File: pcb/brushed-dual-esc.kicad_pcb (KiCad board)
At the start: 2 copper layers, 29.5 x 25 mm, 24 parts, among them J1 XT30PW-M, J2 Conn_02x03_Odd_Even, J3 TC2030-NL, J6 XT30PW-F, J7 XT30PW-F, U2 AZ1117-5.0, U3 STM32C011F4Ux, U4 DRV8231ADSGR, U5 TLV77133PDBVR, U6 DRV8231ADSGR

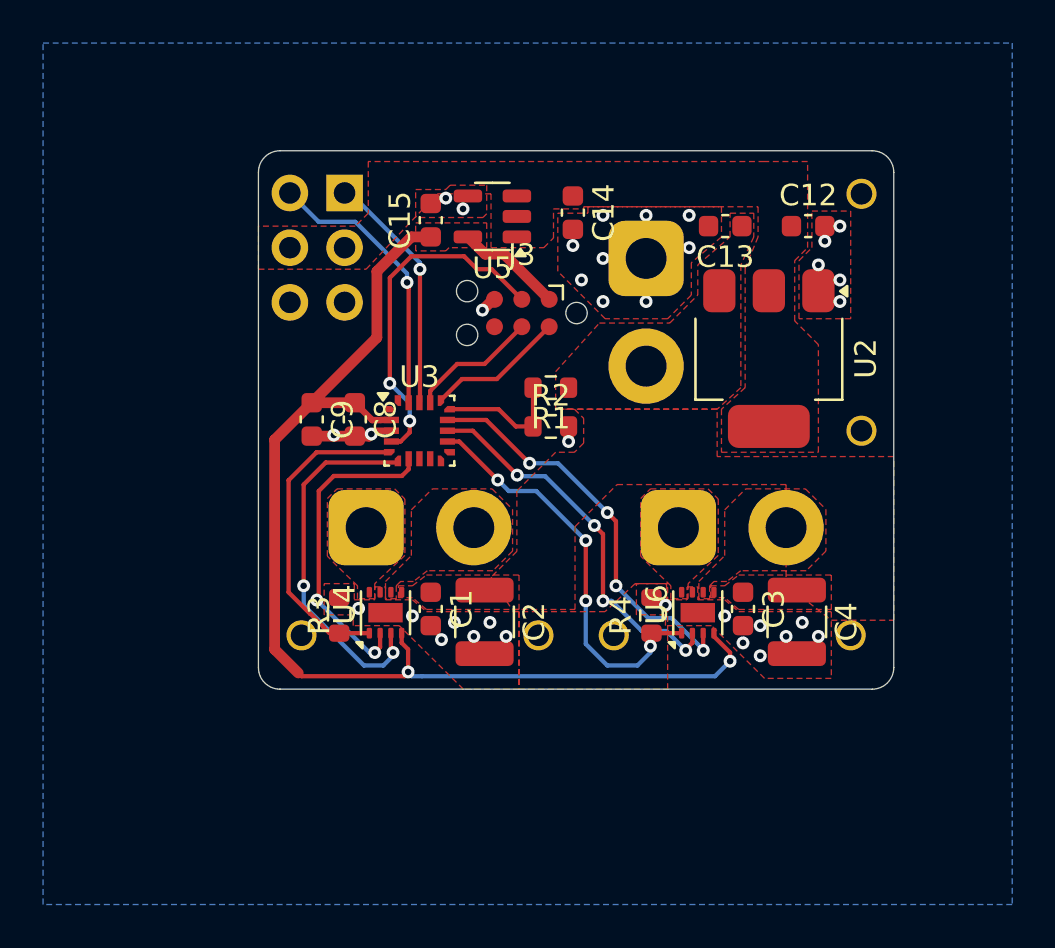
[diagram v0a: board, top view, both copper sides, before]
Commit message: Add status LED on spare pin
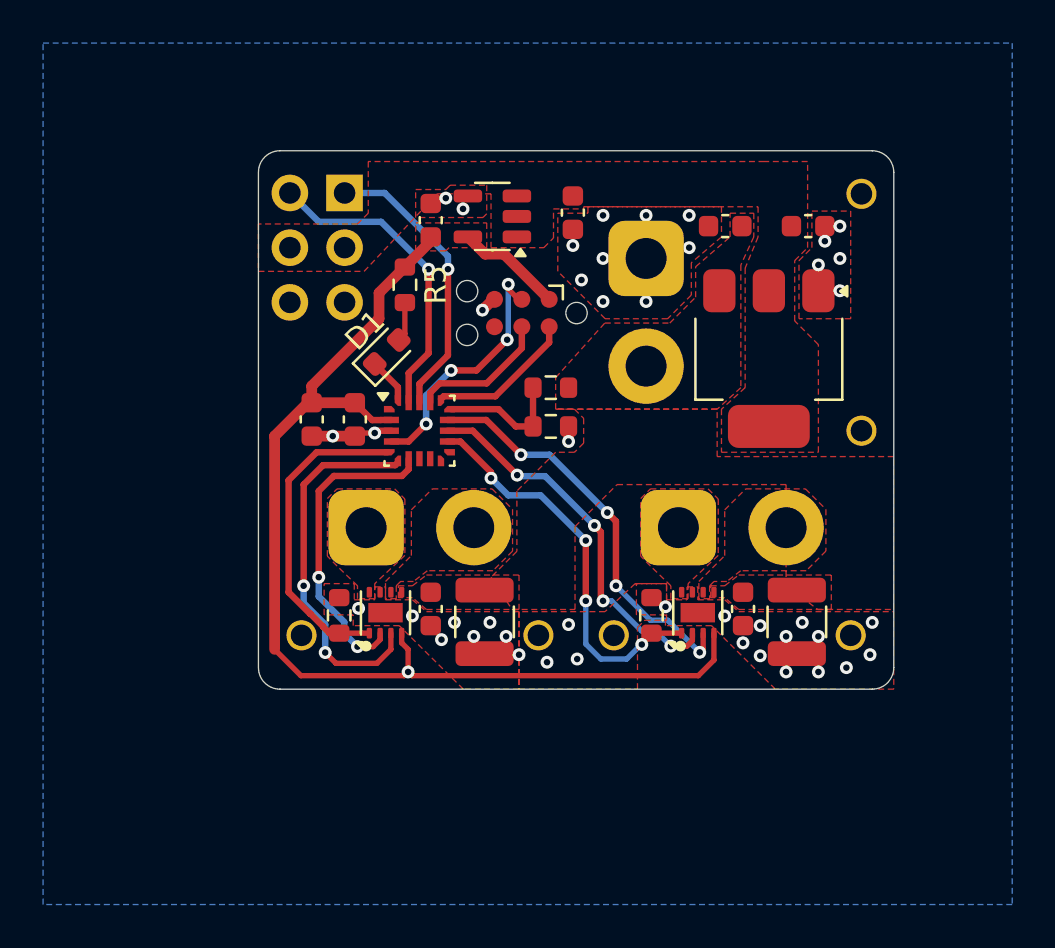
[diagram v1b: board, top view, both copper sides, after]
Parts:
- added D1: B1911USD, LED_SMD:LED_0603_1608Metric, F.Cu at (126.0, 84.3)
- added R5: 270, Resistor_SMD:R_0603_1608Metric, F.Cu at (126.8, 81.2)
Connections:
- J6 pad : GND -> (no net)
- J7 pad : GND -> (no net)
- U3 pad 20: unconnected-(U3-PC14-Pad20) -> /LED
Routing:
- net /~{RESET}: track 16.0 -> 11.9 mm, vias 2 -> 4
- net /LED: track 0.00 -> 2.07 mm
- net /RX_CH2: track 11.4 -> 13.4 mm
- net Net-(D1-A): track 0.00 -> 1.85 mm
- net +3V3: track 57.4 -> 55.9 mm, vias 2 -> 1
- net /RX_CH1: track 13.1 -> 14.5 mm
- net /DRV2_ISENSE: track 19.1 -> 18.6 mm
- net /SWCLK: track 6.04 -> 6.57 mm
- net GND: track 5.31 -> 5.34 mm, vias 35 -> 44

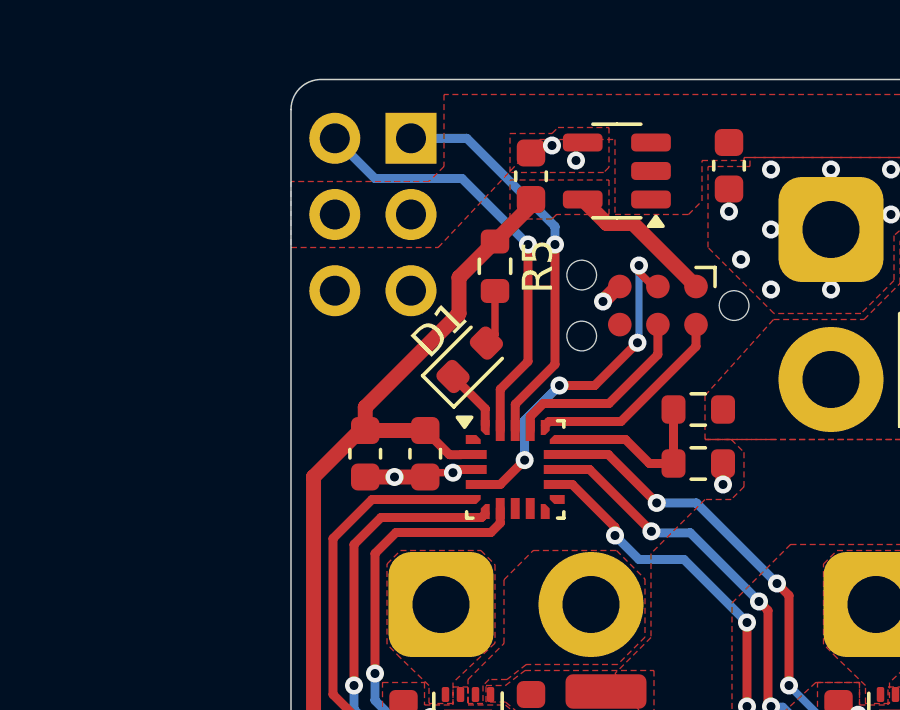
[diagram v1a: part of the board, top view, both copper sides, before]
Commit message: Create 3V3 zone in top left
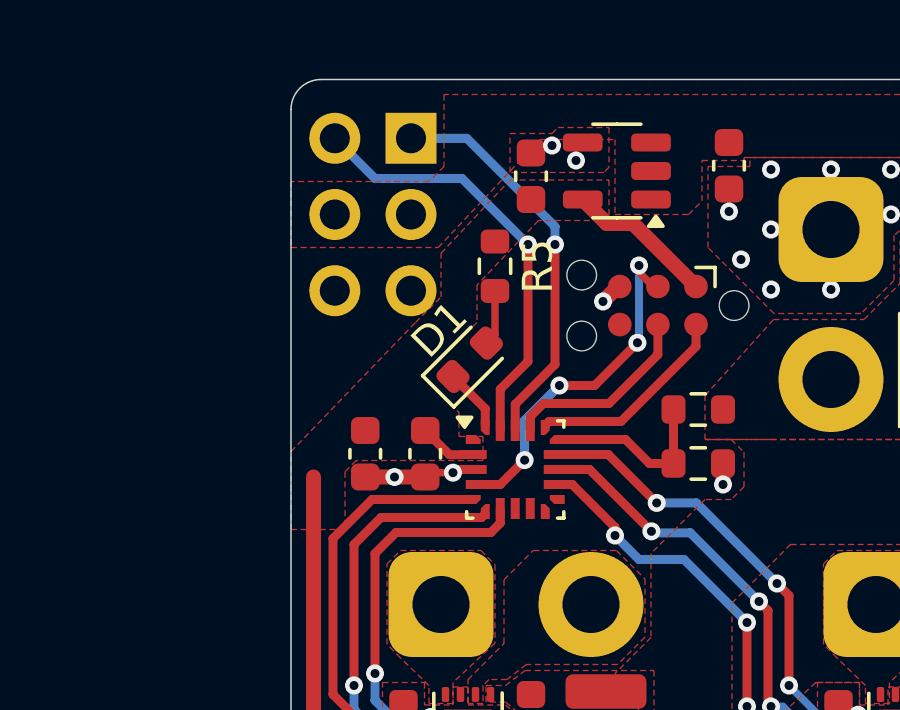
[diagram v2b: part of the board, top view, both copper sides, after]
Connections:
- J6 pad : (no net) -> GND
- J7 pad : (no net) -> GND
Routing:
- net +3V3: track 55.9 -> 41.9 mm

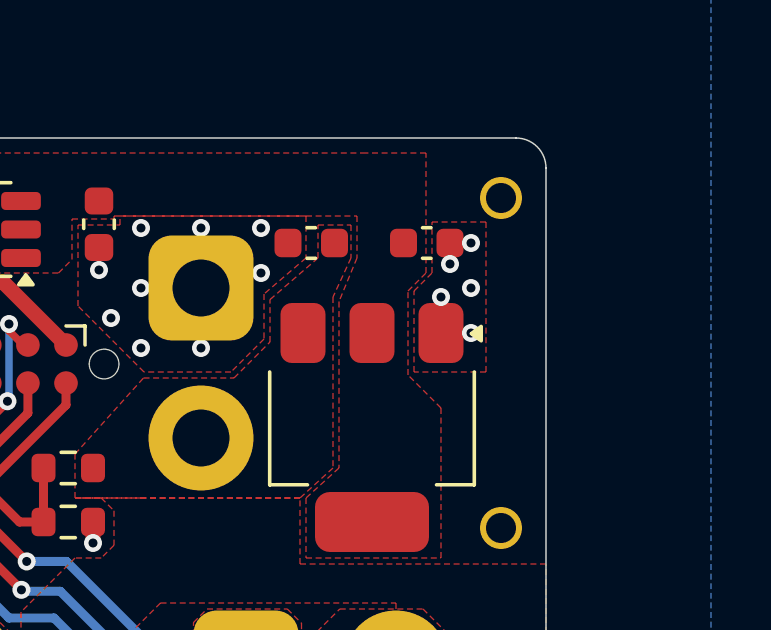
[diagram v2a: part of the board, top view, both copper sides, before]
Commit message: Adjust 5V LDO ground plane placement
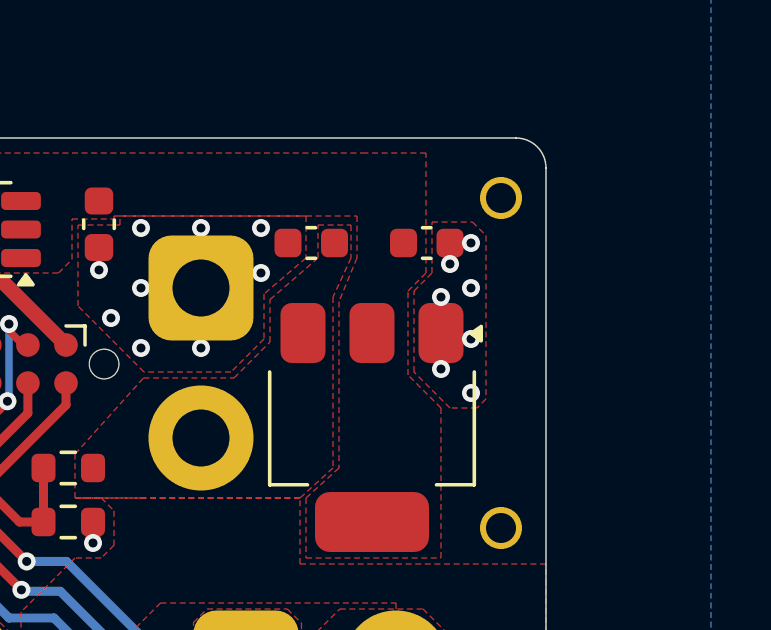
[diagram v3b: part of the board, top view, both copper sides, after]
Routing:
- net GND: vias 44 -> 46

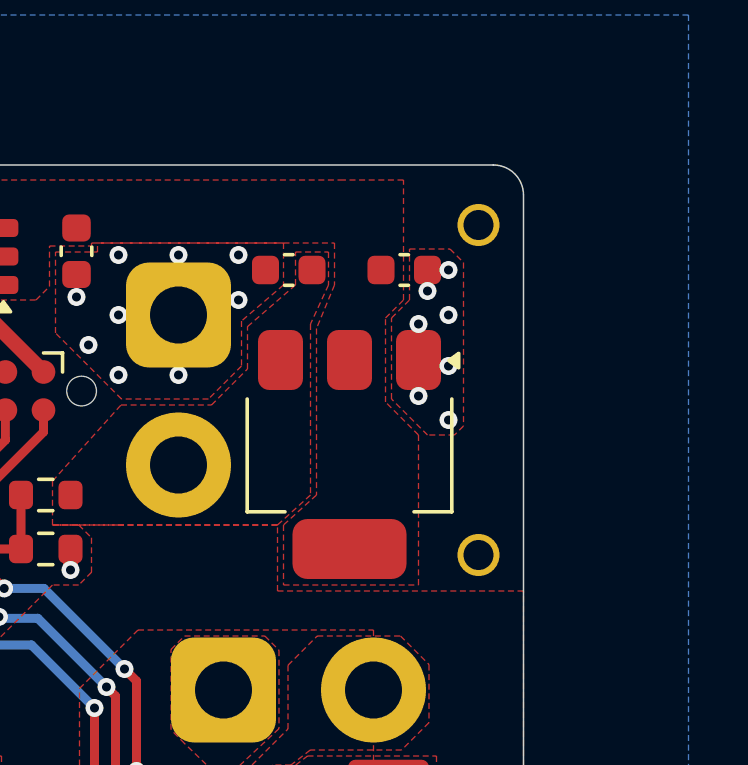
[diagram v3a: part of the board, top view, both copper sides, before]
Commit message: Increase top GND zone size for LDO
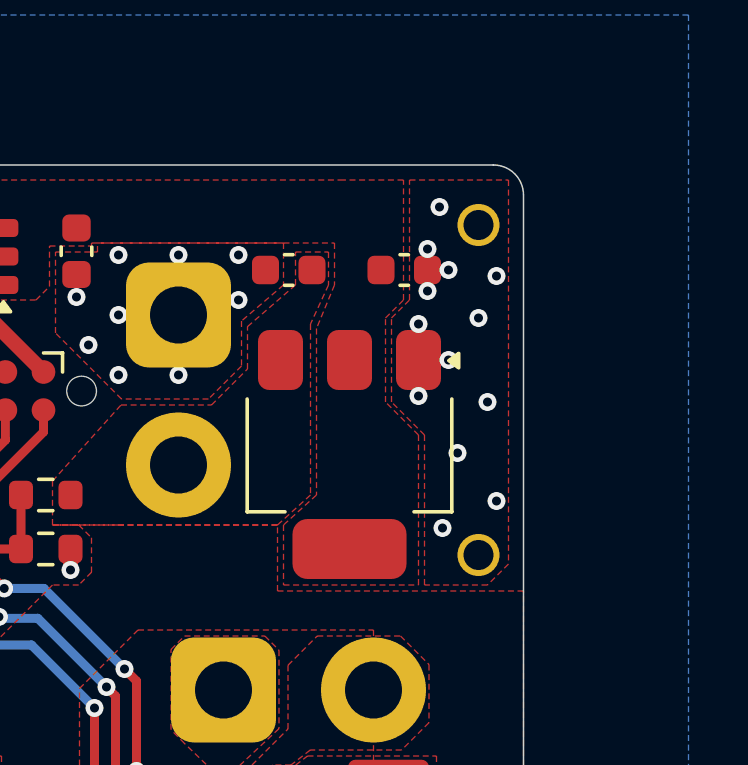
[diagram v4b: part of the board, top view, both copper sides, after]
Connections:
- J1 pad : (no net) -> GND
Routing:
- net GND: vias 46 -> 52

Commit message: Fix capacitor siutation
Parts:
- removed the C1 at (128.0, 96.3)
- removed the C3 at (142.5, 96.3)
- removed C4: 47u, Capacitor_SMD:C_1210_3225Metric
- added C10: UMK107BJ105KA-T, Capacitor_SMD:C_0603_1608Metric, F.Cu at (142.6, 96.4)
- added C11: UMK107BJ105KA-T, Capacitor_SMD:C_0603_1608Metric, F.Cu at (144.3, 96.4)
- added C12: UMK107BJ105KA-T, Capacitor_SMD:C_0603_1608Metric, F.Cu at (146.0, 96.4)
- added C13: UMK107BJ105KA-T, Capacitor_SMD:C_0603_1608Metric, F.Cu at (128.0, 78.2)
- added C16: UMK107BJ105KA-T, Capacitor_SMD:C_0603_1608Metric, F.Cu at (124.0, 87.3)
- added C17: UMK107BJ105KA-T, Capacitor_SMD:C_0603_1608Metric, F.Cu at (122.0, 87.3)
- added C7: UMK107BJ105KA-T, Capacitor_SMD:C_0603_1608Metric, F.Cu at (128.1, 96.4)
- added G***: LOGO, LOGO, B.Cu at (134.6, 89.3)
- added kibuzzard-68AE1D03: G***, kibuzzard-68AE1D03, B.Cu at (127.7, 82.0)
- added kibuzzard-68AE1D1E: G***, kibuzzard-68AE1D1E, B.Cu at (127.7, 79.5)
- added kibuzzard-68AE1D34: G***, kibuzzard-68AE1D34, B.Cu at (121.5, 85.8)
- added kibuzzard-68AE1D4C: G***, kibuzzard-68AE1D4C, B.Cu at (124.0, 85.8)
- added kibuzzard-68AE1DA9: G***, kibuzzard-68AE1DA9, B.Cu at (127.7, 77.0)
- added kibuzzard-68AE251B: G***, kibuzzard-68AE251B, F.Cu at (139.8, 89.8)
- added kibuzzard-68AE2565: G***, kibuzzard-68AE2565, F.Cu at (142.8, 76.5)
- added kibuzzard-68AE2599: G***, kibuzzard-68AE2599, F.Cu at (147.9, 92.5)
- added kibuzzard-68AE2599: G***, kibuzzard-68AE2599, F.Cu at (133.4, 92.5)
- C1: renamed from C13; value 22u -> 22u 16V
- C14, C15: value 1u -> UMK107BJ105KA-T
- C2: value 47u -> ESS107M016AC2KA; footprint Capacitor_SMD:C_1210_3225Metric -> Capacitor_THT:CP_Radial_D5.0mm_P2.00mm; moved to B.Cu
- C3: renamed from C12; value 22u -> 22u 16V
- C8: value 100n -> UMK107BJ105KA-T
- C9: value 4.7u -> UMK107BJ105KA-T
- moved C2 14.3 mm to (135.5, 83.5), turned to 90 degrees
- moved C9 12.7 mm to (131.5, 96.4)
- moved C8 10.4 mm to (129.8, 96.4)
- moved C15 9.27 mm to (126.0, 87.3), turned to -90 degrees
- moved R1 4.20 mm to (124.2, 84.5), turned to 0 degrees
- moved U3 1.82 mm to (129.0, 87.0)
- moved D1 1.04 mm to (126.7, 83.6), turned to 90 degrees
- moved U1 0.70 mm to (143.7, 84.0)
- moved J2 0.59 mm to (131.6, 82.5)
- moved U2 0.30 mm to (131.2, 78.0)
- moved R2 0.21 mm to (133.6, 86.2)
- moved C1 0.10 mm to (141.6, 78.5)
- moved R3 0.05 mm to (133.6, 87.8)
- renumbered J3 to J2, J2 to J3, J6 to J4, J7 to J5, R5 to R1, R1 to R2, R2 to R3, R3 to R4, R4 to R5, U2 to U1, U5 to U2, U6 to U5
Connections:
- C8 pad 1: +3V3 -> +BATT
- C9 pad 1: +3V3 -> +BATT
- U3 pad 1: unconnected-(U3-PC15-Pad1) -> /LED
- U3 pad 20: /LED -> unconnected-(U3-PC14-Pad20)
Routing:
- net +3V3: track 41.9 -> 60.6 mm
- net /SWCLK: track 6.57 -> 3.48 mm
- net /SWDIO: track 6.84 -> 3.89 mm
- net /~{RESET}: track 11.9 -> 9.16 mm, vias 4 -> 2
- net /RX_CH2: track 13.4 -> 11.1 mm
- net GND: track 5.34 -> 7.49 mm, vias 52 -> 47
- net /DRV1_IN2: track 14.5 -> 16.6 mm
- net /DRV1_ISENSE: track 14.9 -> 16.8 mm
- net /DRV1_IN1: track 17.3 -> 19.2 mm
- net /BATT_SENSE: track 5.93 -> 4.01 mm
- net /RX_CH1: track 14.5 -> 12.7 mm
- net Net-(D1-A): track 1.85 -> 2.39 mm

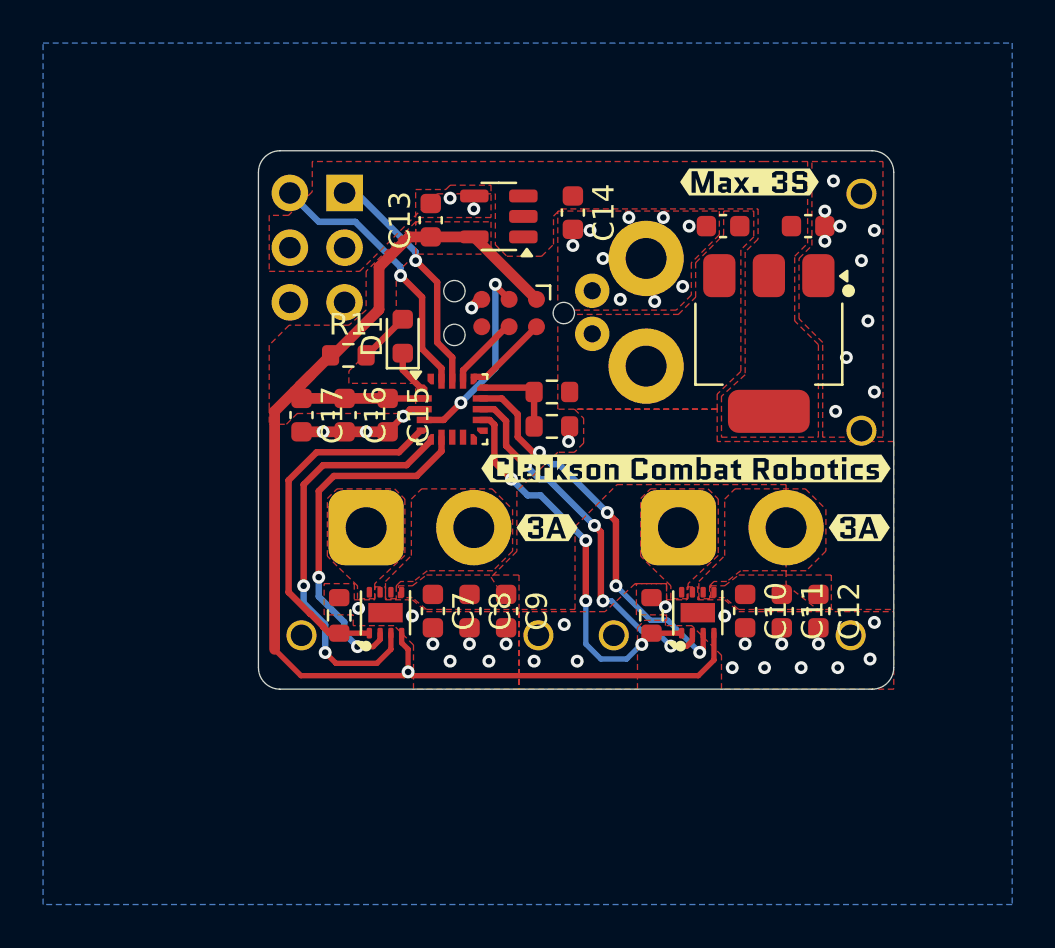
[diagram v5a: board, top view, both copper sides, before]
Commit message: Add testpoints and imrpove silkscreen
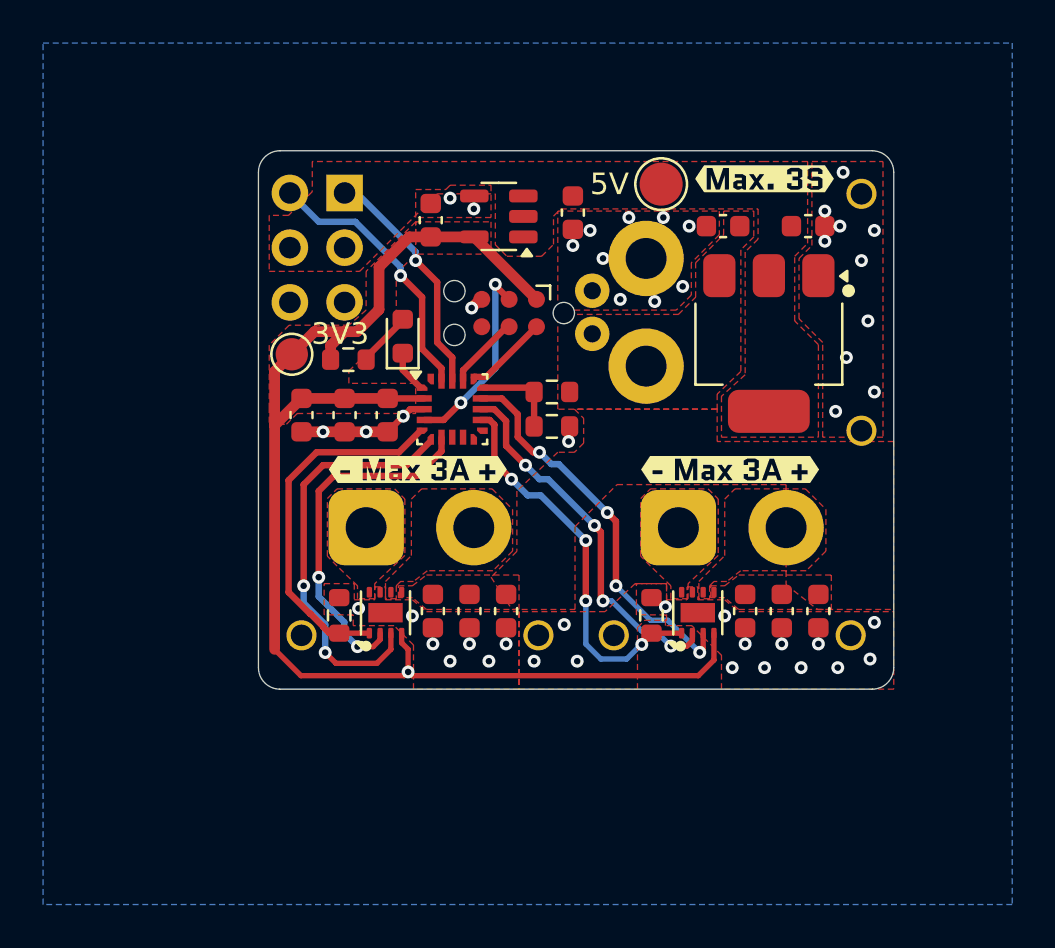
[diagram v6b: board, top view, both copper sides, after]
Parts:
- removed kibuzzard-68AE251B: G***, kibuzzard-68AE251B
- removed kibuzzard-68AE2599 (x2): G***, kibuzzard-68AE2599
- added TP1: 5V, TestPoint:TestPoint_Pad_D2.0mm, F.Cu at (138.7, 76.5)
- added TP2: 3V3, TestPoint:TestPoint_Pad_D1.5mm, F.Cu at (121.5, 84.5)
- added kibuzzard-68AE6F6F: G***, kibuzzard-68AE6F6F, B.Cu at (128.1, 86.1)
- added kibuzzard-68AF2469: G***, kibuzzard-68AF2469, F.Cu at (141.9, 89.8)
- added kibuzzard-68AF2469: G***, kibuzzard-68AF2469, F.Cu at (127.4, 89.8)
- added kibuzzard-68AF2501: G***, kibuzzard-68AF2501, B.Cu at (138.7, 76.3)
- moved kibuzzard-68AE2565 0.72 mm to (143.5, 76.3)
- moved R1 0.20 mm to (124.2, 84.7)
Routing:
- net +3V3: track 60.6 -> 63.8 mm

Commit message: Add step file
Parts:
- removed the C11 at (144.3, 96.4)
- removed the C8 at (129.8, 96.4)
- removed kibuzzard-68AE1D03: G***, kibuzzard-68AE1D03
- removed kibuzzard-68AE1D1E: G***, kibuzzard-68AE1D1E
- removed kibuzzard-68AE1D34: G***, kibuzzard-68AE1D34
- removed kibuzzard-68AE1D4C: G***, kibuzzard-68AE1D4C
- removed kibuzzard-68AE1DA9: G***, kibuzzard-68AE1DA9
- removed kibuzzard-68AE2565: G***, kibuzzard-68AE2565
- removed kibuzzard-68AE6F6F: G***, kibuzzard-68AE6F6F
- removed kibuzzard-68AF2501: G***, kibuzzard-68AF2501
- C1, C3: footprint Capacitor_SMD:C_0603_1608Metric -> Capacitor_SMD:C_0805_2012Metric
- moved C5 12.5 mm to (133.7, 95.9), turned to 0 degrees
- moved C1 8.93 mm to (142.3, 87.4), turned to 0 degrees
- moved TP1 6.91 mm to (145.6, 77.0)
- moved G*** 6.28 mm to (128.8, 86.9)
- moved C3 4.63 mm to (141.1, 77.2), turned to -90 degrees
- moved C10 2.04 mm to (144.6, 97.0)
- moved R5 2.04 mm to (140.2, 97.2)
- moved U5 2.04 mm to (142.3, 97.0)
- moved U1 1.63 mm to (144.4, 82.5), turned to 0 degrees
- moved R2 1.51 mm to (133.8, 84.7)
- moved R3 1.51 mm to (133.8, 86.3)
- moved R4 1.12 mm to (124.7, 97.2)
- moved U4 1.12 mm to (126.8, 97.0)
- moved J4 1.12 mm to (124.5, 93.5)
- moved J5 1.12 mm to (140.0, 93.5)
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- renumbered C9 to C11, C14 to C2, C13 to C4, C2 to C5, C15 to C6, C16 to C7, C17 to C8, C7 to C9
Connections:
- J1 pad : GND -> (no net)
- J4 pad : GND -> (no net)
- J5 pad : GND -> (no net)
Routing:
- net +3V3: track 63.8 -> 73.9 mm, vias 1 -> 2
- net /DRV1_IN2: track 16.6 -> 20.0 mm, vias 2 -> 0
- net /DRV2_IN1: track 18.4 -> 21.6 mm
- net /DRV2_IN2: track 17.3 -> 19.8 mm
- net /~{RESET}: track 9.16 -> 11.1 mm, vias 2 -> 4
- net /DRV1_IN1: track 19.2 -> 20.6 mm
- net /DRV1_ISENSE: track 16.8 -> 15.7 mm, vias 0 -> 3
- net GND: track 7.49 -> 8.17 mm, vias 47 -> 36
- net /DRV2_ISENSE: track 18.3 -> 18.9 mm
- net /SWCLK: track 3.48 -> 4.05 mm
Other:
- board text added: "3V3"
- board text added: "5V 1A"
- board text added: "CH1"
- board text added: "CH2"
- board text added: "Clarkson"
- board text added: "Combat Robotics"
- board text added: "Designed by Sigmond Kukla in 2025"
- board text added: "GND"
- board text added: "JLCJLCJLCJLC"
- board text added: "SIG"
- board text added: "University"
